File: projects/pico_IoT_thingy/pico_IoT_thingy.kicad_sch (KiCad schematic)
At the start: 58 parts, among them IC1 THVD1406DR, J1 Barrel_Jack_Switch, J2 QWIIC, J3 Conn_01x03, J4 Screw_Terminal_01x03, J5 Screw_Terminal_01x04, J6 Conn_02x05_Odd_Even, J7 Conn_01x02, K1 RT314A05, Q1 BC817, SW1 SW_SPST, SW2 SW_SPST, SW3 SW_DIP_x04, U1 TSR_1-2450, U2 SHT31-DIS, U3 TLV1117-33

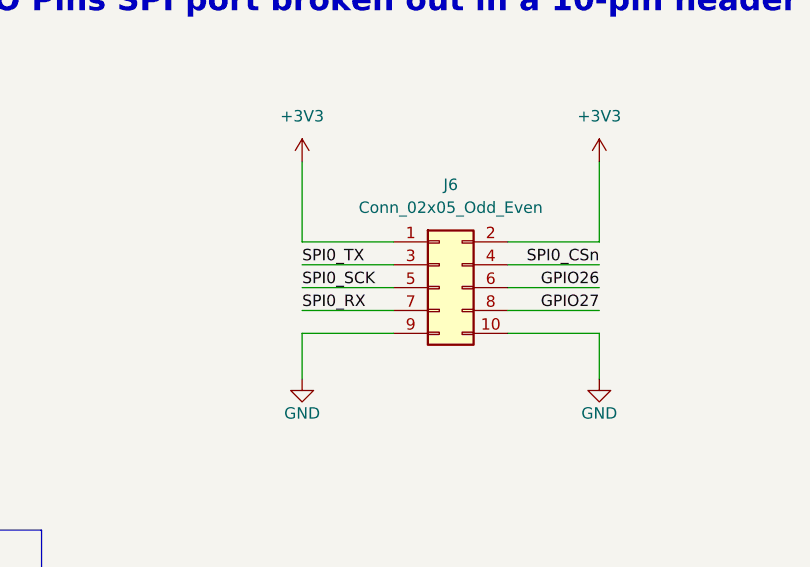
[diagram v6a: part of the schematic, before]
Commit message: Pico IoT thingy - initial placement of components in PCB
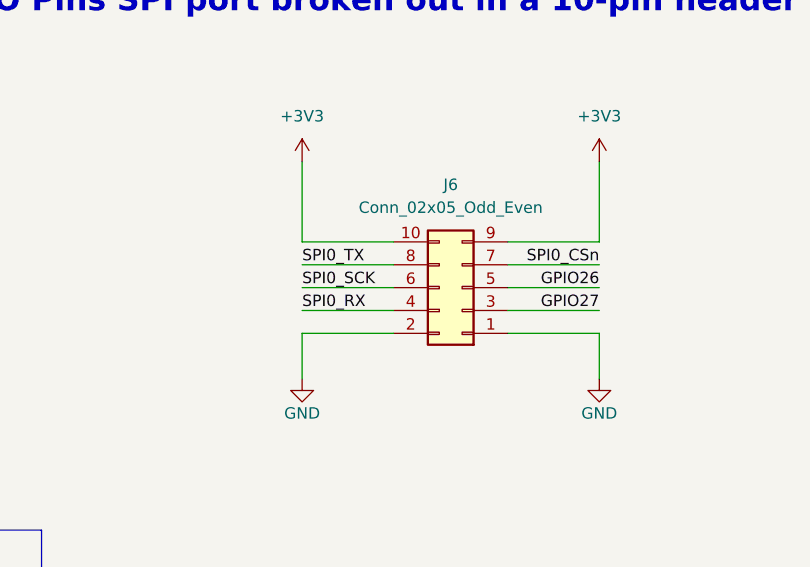
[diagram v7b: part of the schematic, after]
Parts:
- J3: footprint Connector_PinHeader_2.54mm:PinHeader_1x03_P2.54mm_Horizontal -> Connector_PinHeader_2.54mm:PinHeader_1x03_P2.54mm_Vertical
- SW1, SW2: footprint Button_Switch_SMD:SW_SPST_Omron_B3FS-101xP -> Button_Switch_SMD:SW_Tactile_SPST_NO_Straight_CK_PTS636Sx25SMTRLFS
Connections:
- net +3V3: now also J6.10 (Pin_10), J6.9 (Pin_9); no longer J6.1 (Pin_1), J6.2 (Pin_2)
- net GND: now also J6.1 (Pin_1), J6.2 (Pin_2); no longer J6.10 (Pin_10), J6.9 (Pin_9)
- net GPIO26: now also J6.5 (Pin_5); no longer J6.6 (Pin_6)
- net GPIO27: now also J6.3 (Pin_3); no longer J6.8 (Pin_8)
- net SPI0_CSn: now also J6.7 (Pin_7); no longer J6.4 (Pin_4)
- net SPI0_RX: now also J6.4 (Pin_4); no longer J6.7 (Pin_7)
- net SPI0_SCK: now also J6.6 (Pin_6); no longer J6.5 (Pin_5)
- net SPI0_TX: now also J6.8 (Pin_8); no longer J6.3 (Pin_3)
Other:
- moved on the sheet: J6
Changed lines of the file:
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@@
 	(wire
 		(pts
+			(xy 328.93 220.98) (xy 339.09 220.98)
+		)
+		(stroke
+			(width 0)
+			(type default)
+		)
+	)
+	(wire
+		(pts
 			(xy 68.58 248.92) (xy 68.58 251.46)
 		)
@@
 	(wire
 		(pts
-			(xy 339.09 231.14) (xy 328.93 231.14)
-		)
-		(stroke
-			(width 0)
-			(type default)
-		)
-	)
-	(wire
-		(pts
 			(xy 64.77 152.4) (xy 64.77 154.94)
 		)
@@
 	(wire
 		(pts
+			(xy 328.93 231.14) (xy 339.09 231.14)
+		)
+		(stroke
+			(width 0)
+			(type default)
+		)
+	)
+	(wire
+		(pts
 			(xy 377.19 60.96) (xy 377.19 67.31)
 		)
@@
 	(wire
 		(pts
-			(xy 339.09 220.98) (xy 328.93 220.98)
-		)
-		(stroke
-			(width 0)
-			(type default)
-		)
-	)
-	(wire
-		(pts
 			(xy 351.79 220.98) (xy 361.95 220.98)
 		)
@@
 			)
 		)
-		(property "Footprint" "Connector_PinHeader_2.54mm:PinHeader_1x03_P2.54mm_Horizontal"
+		(property "Footprint" "Connector_PinHeader_2.54mm:PinHeader_1x03_P2.54mm_Vertical"
 			(at 171.45 88.9 0)
 			(effects
@@
 	(symbol
 		(lib_id "Connector_Generic:Conn_02x05_Odd_Even")
-		(at 344.17 226.06 0)
+		(at 346.71 226.06 180)
 		(unit 1)
 		(exclude_from_sim no)
@@
 		)
 		(property "Footprint" "Connector_PinHeader_2.54mm:PinHeader_2x05_P2.54mm_Vertical"
-			(at 344.17 226.06 0)
+			(at 346.71 226.06 0)
 			(effects
 				(font
@@
 		)
 		(property "Datasheet" "~"
-			(at 344.17 226.06 0)
+			(at 346.71 226.06 0)
 			(effects
 				(font
@@
 		)
 		(property "Description" "Generic connector, double row, 02x05, odd/even pin numbering scheme (row 1 odd numbers, row 2 even numbers), script generated (kicad-library-utils/schlib/autogen/connector/)"
-			(at 344.17 226.06 0)
+			(at 346.71 226.06 0)
 			(effects
 				(font
@@
 			)
 		)
-		(property "Footprint" "Button_Switch_SMD:SW_SPST_Omron_B3FS-101xP"
+		(property "Footprint" "Button_Switch_SMD:SW_Tactile_SPST_NO_Straight_CK_PTS636Sx25SMTRLFS"
 			(at 54.61 162.56 0)
 			(effects
@@
 			)
 		)
-		(property "Datasheet" "~"
+		(property "Datasheet" "https://www.mouser.com/catalog/specsheets/omron_B3FS.pdf"
 			(at 54.61 162.56 0)
 			(effects
@@
 			)
 		)
-		(property "Footprint" "Button_Switch_SMD:SW_SPST_Omron_B3FS-101xP"
+		(property "Footprint" "Button_Switch_SMD:SW_Tactile_SPST_NO_Straight_CK_PTS636Sx25SMTRLFS"
 			(at 167.64 110.49 0)
 			(effects
@@
 			)
 		)
-		(property "Datasheet" "~"
+		(property "Datasheet" "https://www.mouser.com/catalog/specsheets/omron_B3FS.pdf"
 			(at 167.64 110.49 0)
 			(effects

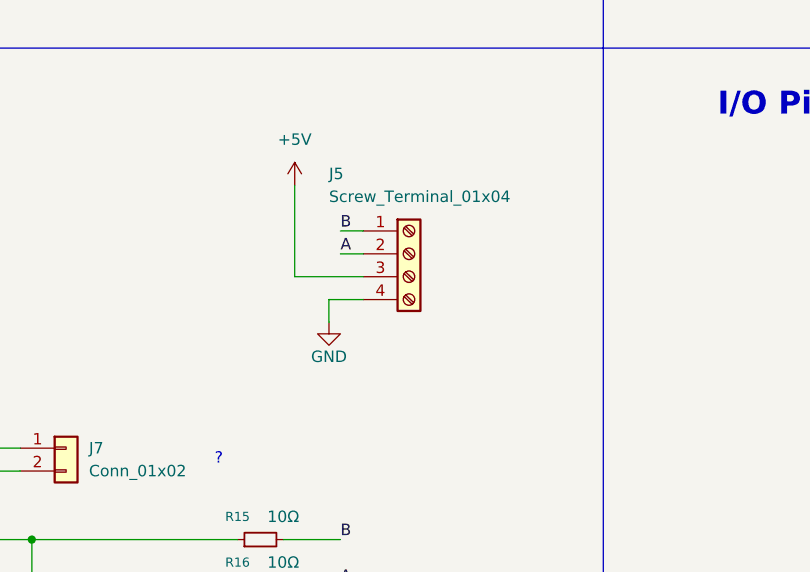
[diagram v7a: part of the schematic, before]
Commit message: Pico IoT thingy - Flip 1x04 screw terminal to have GND on Pin 1, add 3Ds
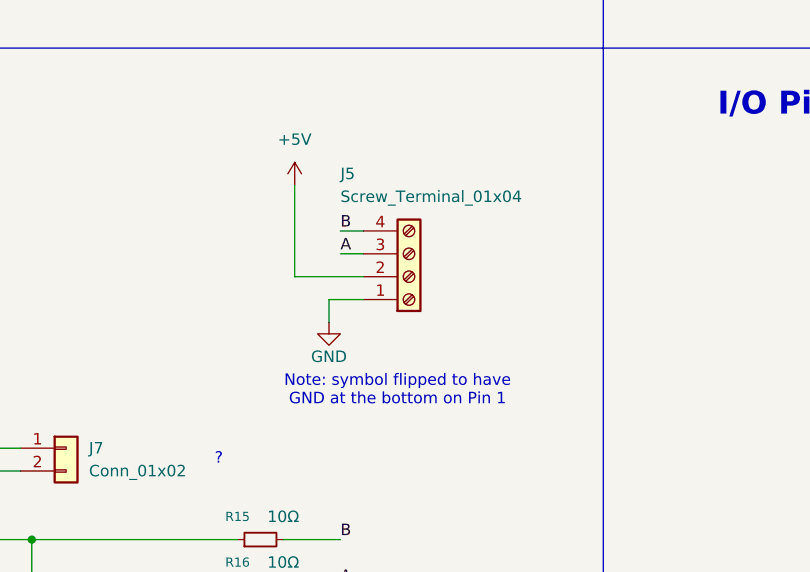
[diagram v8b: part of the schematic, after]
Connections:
- net +5V: now also J5.2 (Pin_2); no longer J5.3 (Pin_3)
- net A: now also J5.3 (Pin_3); no longer J5.2 (Pin_2)
- net B: now also J5.4 (Pin_4); no longer J5.1 (Pin_1)
- net GND: now also J5.1 (Pin_1); no longer J5.4 (Pin_4)
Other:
- note added: "Note: symbol flipped to have GND at the bottom on Pin 1"
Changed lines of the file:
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@@
 		)
 	)
+	(text "Note: symbol flipped to have \nGND at the bottom on Pin 1 "
+		(exclude_from_sim no)
+		(at 256.54 226.06 0)
+		(effects
+			(font
+				(size 1.27 1.27)
+			)
+		)
+	)
 	(text "RS485 connector"
 		(exclude_from_sim no)
@@
 	(symbol
 		(lib_id "Connector:Screw_Terminal_01x04")
-		(at 257.81 210.82 0)
+		(at 257.81 213.36 0)
+		(mirror x)
 		(unit 1)
 		(exclude_from_sim no)
@@
 		(dnp no)
 		(property "Reference" "J5"
-			(at 248.92 201.93 0)
+			(at 250.19 201.93 0)
 			(effects
 				(font
@@
 		)
 		(property "Value" "Screw_Terminal_01x04"
-			(at 248.92 204.47 0)
+			(at 250.19 204.47 0)
 			(effects
 				(font
@@
 		)
 		(property "Footprint" "TerminalBlock:TerminalBlock_MaiXu_MX126-5.0-04P_1x04_P5.00mm"
-			(at 257.81 210.82 0)
+			(at 257.81 213.36 0)
 			(effects
 				(font
@@
 		)
 		(property "Datasheet" "~"
-			(at 257.81 210.82 0)
+			(at 257.81 213.36 0)
 			(effects
 				(font
@@
 		)
 		(property "Description" "Generic screw terminal, single row, 01x04, script generated (kicad-library-utils/schlib/autogen/connector/)"
-			(at 257.81 210.82 0)
+			(at 257.81 213.36 0)
 			(effects
 				(font
